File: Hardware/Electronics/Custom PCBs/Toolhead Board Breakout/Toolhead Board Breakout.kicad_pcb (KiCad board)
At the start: 2 copper layers, 75 x 75 mm, 31 parts, among them J1 Conn_02x08_Odd_Even, J10 Conn_01x03, J11 Conn_01x03, J12 Conn_01x03, J13 Conn_01x02, J14 Conn_01x04, J15 Conn_01x02, J16 Conn_01x04, J17 Conn_01x02, J18 Conn_01x02, J19 Conn_01x04, J2 Conn_02x08_Odd_Even, J20 Conn_01x04, J21 Conn_01x02, J22 Conn_01x04, J3 Conn_02x08_Odd_Even, J4 Conn_02x04_Odd_Even, J5 Conn_02x04_Odd_Even, J6 Conn_01x04, J7 Conn_01x03, J8 Conn_01x03, J9 Conn_01x03

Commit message: Updated Breakout Board Layout
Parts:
- moved J6 7.46 mm to (104.5, 60.3), turned to -70 degrees
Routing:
- net +24V: track 0.00 -> 45.3 mm
- net +5V: track 0.00 -> 37.8 mm
- net THERM0: track 0.00 -> 34.5 mm, vias 0 -> 1
- net OB2: track 0.00 -> 31.9 mm
- net SERVO3: track 0.00 -> 31.5 mm
- net OA1: track 0.00 -> 30.2 mm
- net SDA: track 0.00 -> 29.9 mm
- net OB1: track 0.00 -> 29.2 mm
- net SCL: track 0.00 -> 29.1 mm
- net SERVO5: track 0.00 -> 28.8 mm
- net D1: track 0.00 -> 27.9 mm
- net SERVO1: track 0.00 -> 27.5 mm
- net SERVO4: track 0.00 -> 27.3 mm
- net OA2: track 0.00 -> 26.0 mm
- net SERVO6: track 0.00 -> 25.0 mm
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
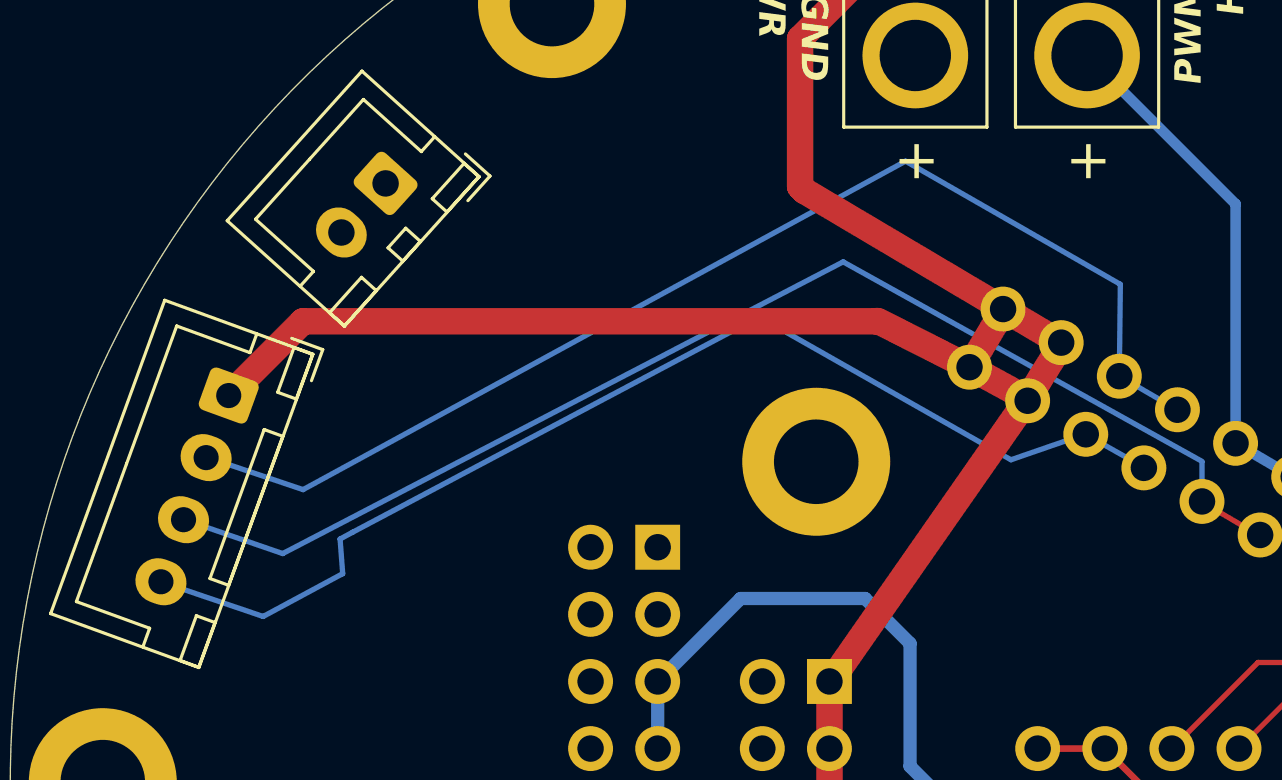
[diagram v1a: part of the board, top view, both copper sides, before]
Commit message: updated breakout board design
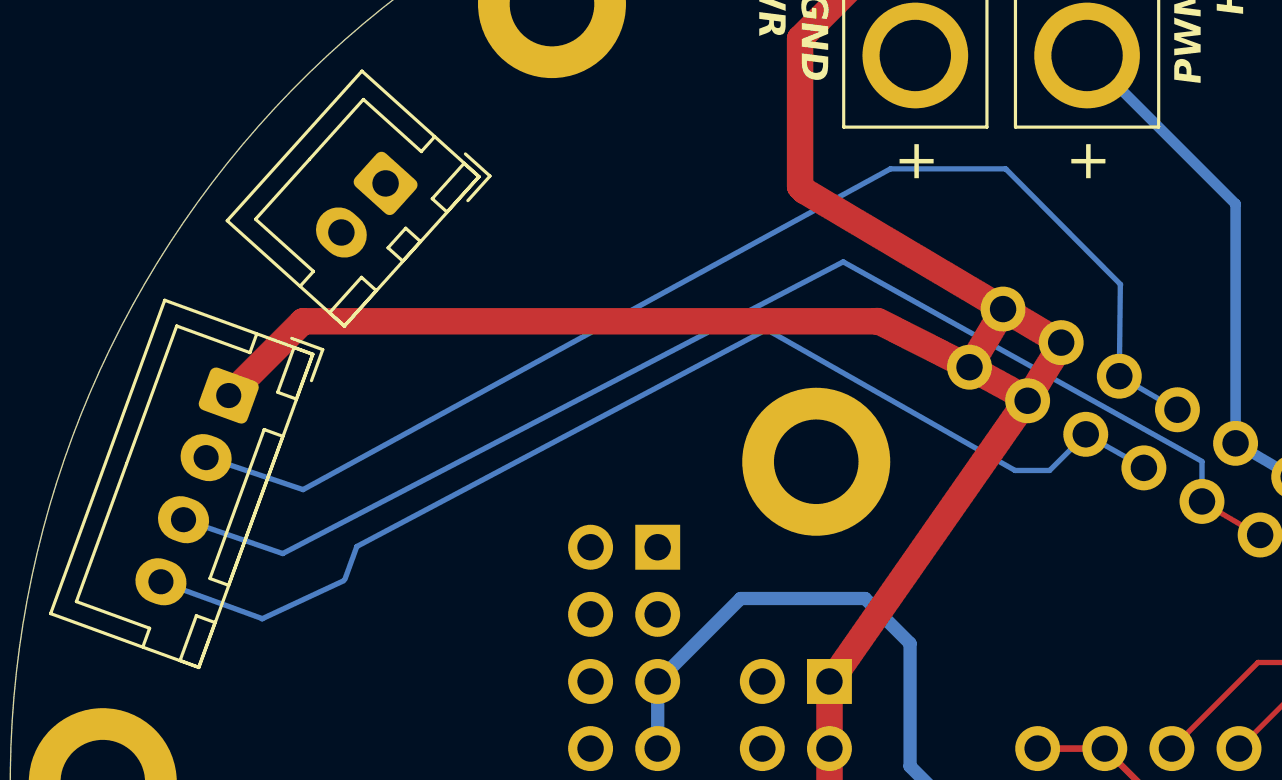
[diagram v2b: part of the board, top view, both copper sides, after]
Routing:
- net 24V_PWM1: track 0.00 -> 4.39 mm
- net 24V_PWM3: track 0.00 -> 3.24 mm
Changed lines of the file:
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@@
-	)
-	(gr_line
-		(start 50.46 65.54)
-		(end 49.98 65.8)
-		(stroke
-			(width 0.2)
-			(type default)
-		)
-		(layer "B.Cu")
-		(net 14)
 	)
 	(gr_line
@@
 	)
 	(gr_line
-		(start 75.37 62.8)
-		(end 65.94 57.45)
+		(start 75.525 63.205)
+		(end 66.095 57.855)
 		(stroke
 			(width 0.2)
@@
 	)
 	(gr_line
-		(start 78.18 61.83)
-		(end 75.37 62.8)
-		(stroke
-			(width 0.2)
-			(type default)
-		)
-		(layer "B.Cu")
-		(net 14)
-	)
-	(gr_line
 		(start 81.48 104.3)
 		(end 81.88 106.7)
@@
 	(gr_line
 		(start 48.58 63.93)
-		(end 71.38 51.5)
+		(end 70.81 51.79)
 		(stroke
 			(width 0.2)
@@
 	(gr_line
 		(start 43.21 67.42)
-		(end 47.07 68.73)
+		(end 47.040409 68.814155)
 		(stroke
 			(width 0.2)
@@
 	)
 	(gr_line
-		(start 71.38 51.5)
-		(end 79.51 56.16)
+		(start 75.19 51.81)
+		(end 79.523089 56.173089)
 		(stroke
 			(width 0.2)
@@
 	)
 	(gr_line
-		(start 50.08 67.11)
-		(end 49.98 65.8)
+		(start 50.165325 67.317289)
+		(end 50.614675 66.08271)
 		(stroke
 			(width 0.2)
@@
 	)
 	(gr_line
-		(start 65.94 57.34)
-		(end 50.46 65.54)
+		(start 66.094675 57.88271)
+		(end 50.614675 66.08271)
 		(stroke
 			(width 0.2)
@@
 	)
 	(gr_line
-		(start 47.07 68.73)
-		(end 50.08 67.11)
+		(start 47.021002 68.822309)
+		(end 50.118998 67.37769)
 		(stroke
 			(width 0.2)
@@
 	)
 	(segment
+		(start 75.17 51.79)
+		(end 75.19 51.81)
+		(width 0.2)
+		(layer "B.Cu")
+		(net 12)
+	)
+	(segment
+		(start 70.81 51.79)
+		(end 75.17 51.79)
+		(width 0.2)
+		(layer "B.Cu")
+		(net 12)
+	)
+	(segment
 		(start 82.599852 64.37667)
 		(end 82.599852 62.890148)
@@
 	)
 	(segment
+		(start 76.832113 63.205)
+		(end 78.200443 61.83667)
+		(width 0.2)
+		(layer "B.Cu")
+		(net 14)
+	)
+	(segment
+		(start 75.525 63.205)
+		(end 76.832113 63.205)
+		(width 0.2)
+		(layer "B.Cu")
+		(net 14)
+	)
+	(segment

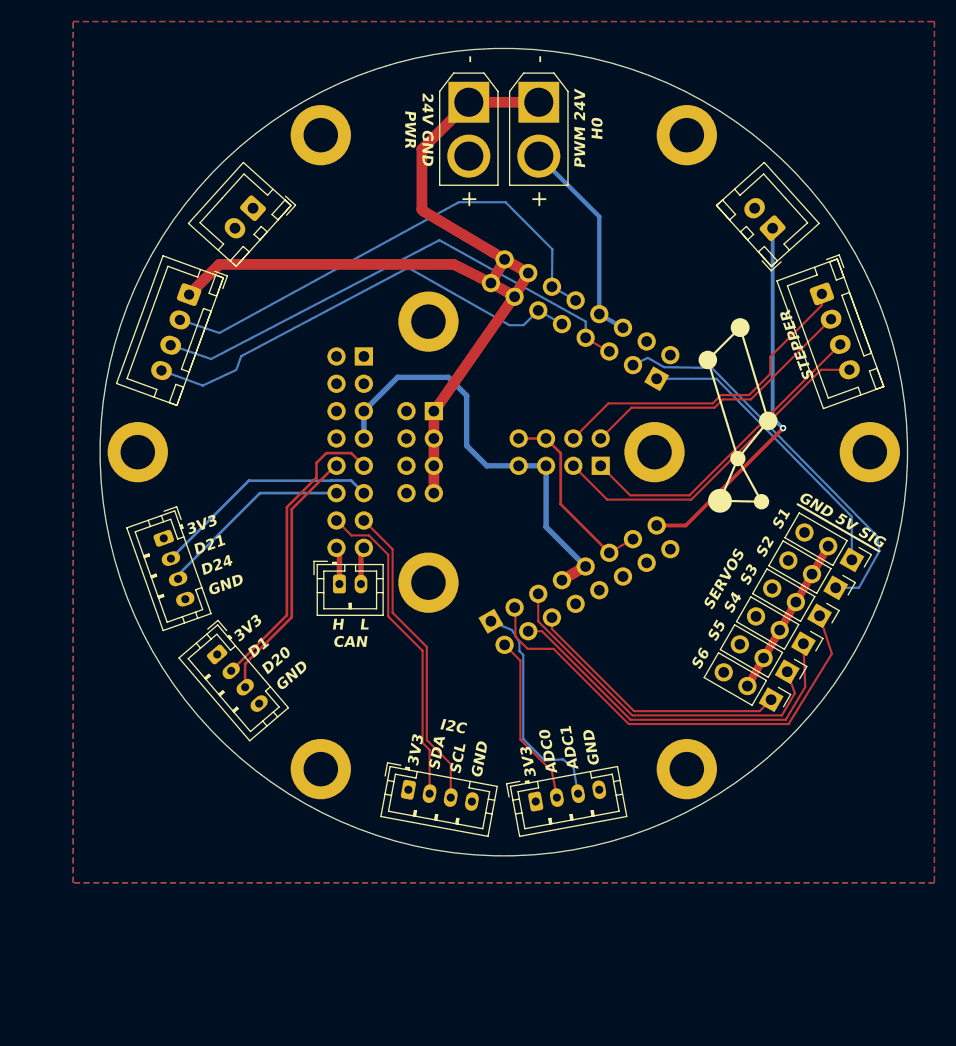
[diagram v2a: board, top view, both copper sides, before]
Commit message: Updated Breakout Board Layout
Finished all the traces. Prior to adding LDO's from 24V to 5V.
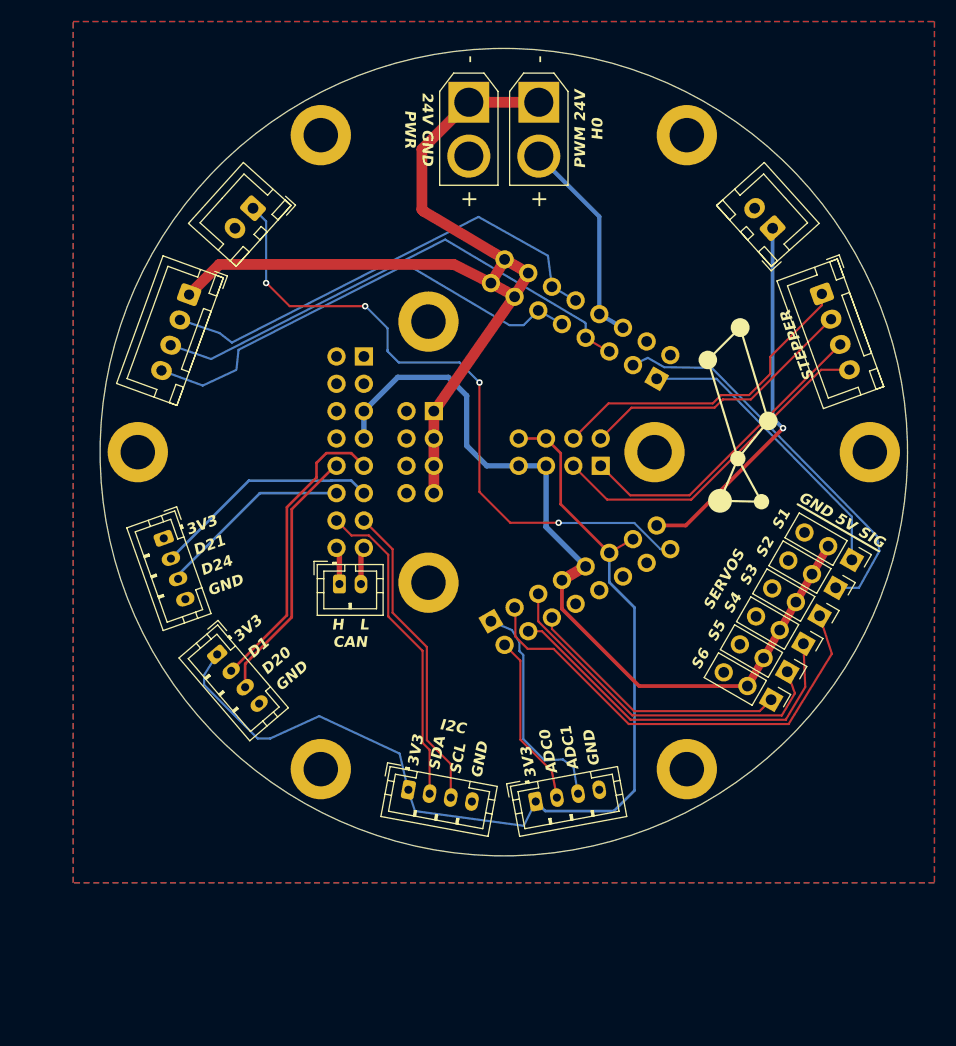
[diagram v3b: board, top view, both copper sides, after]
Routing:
- net THERM1: track 0.00 -> 62.9 mm, vias 0 -> 4
- net +3.3V: track 15.6 -> 58.1 mm
- net +5V: track 37.8 -> 60.6 mm
- net 24V_PWM1: track 4.39 -> 0.00 mm

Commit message: Finished Breakout Board
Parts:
- added C1: 10uF, Capacitor_SMD:C_0805_2012Metric_Pad1.18x1.45mm_HandSolder, F.Cu at (60.0, 54.9)
- added C2: 10uF, Capacitor_SMD:C_0805_2012Metric_Pad1.18x1.45mm_HandSolder, B.Cu at (56.2, 60.1)
- added R1: 5k, Potentiometer_SMD:Potentiometer_Bourns_TC33X_Vertical, F.Cu at (52.3, 60.7)
- added R2: 121, Resistor_SMD:R_0805_2012Metric_Pad1.20x1.40mm_HandSolder, F.Cu at (62.1, 54.9)
- added U1: LM1084-5.0, Package_TO_SOT_SMD:TO-263-3_TabPin2, B.Cu at (51.1, 74.7)
- renumbered H4 to H1, H3 to H1, H8 to H2, H9 to H2, H6 to H2, H7 to H2, H5 to H2
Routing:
- net +5V: track 60.6 -> 92.2 mm, vias 0 -> 3
- net +24V: track 45.3 -> 62.7 mm, vias 0 -> 1
- net Net-(U1-GND): track 0.00 -> 15.5 mm, vias 0 -> 3
- net 24V_PWM1: track 0.00 -> 10.4 mm
- net 24V_PWM2: track 1.49 -> 9.01 mm
- net 24V_PWM3: track 3.24 -> 9.32 mm
- net THERM1: track 62.9 -> 59.7 mm
- net D21: track 21.4 -> 22.3 mm

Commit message: Breakout Board fix
About 60% finished but need some help
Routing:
- net +5V: track 92.2 -> 109.9 mm
- net Net-(U1-GND): track 15.5 -> 14.2 mm

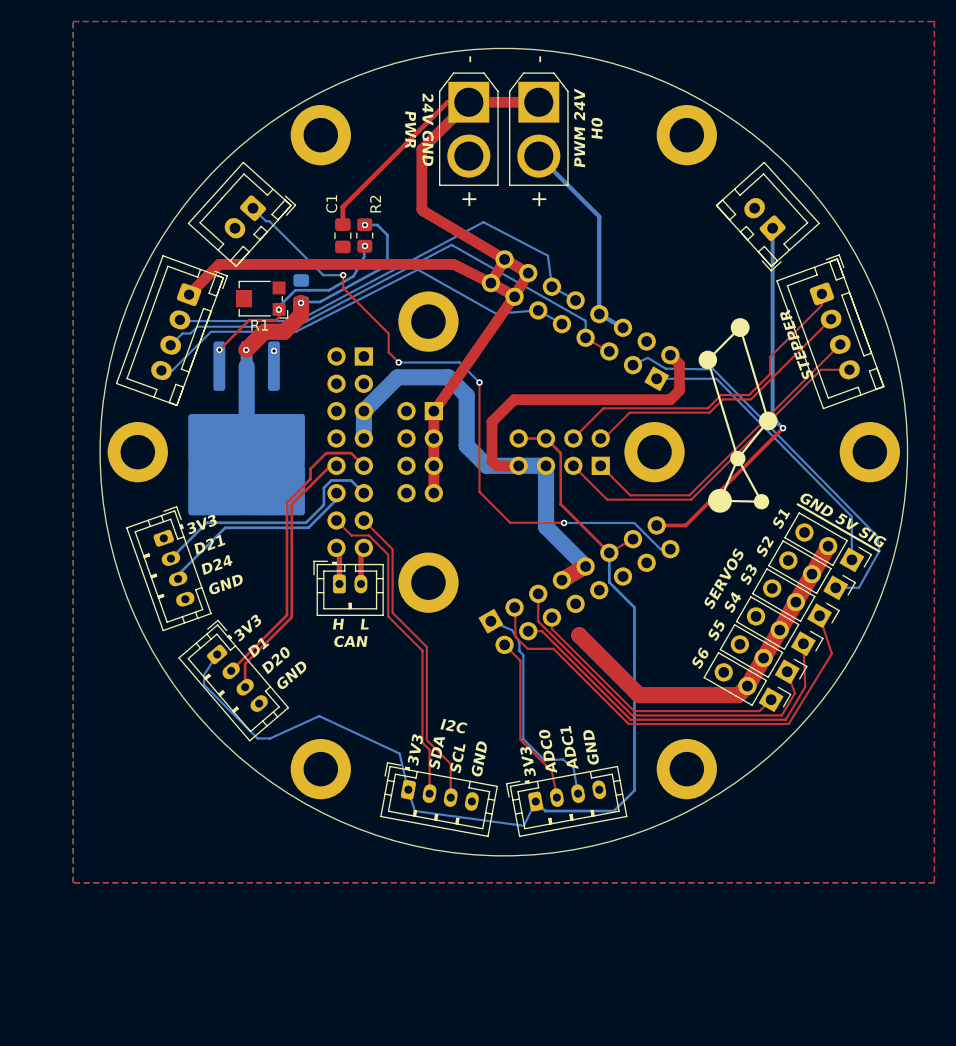
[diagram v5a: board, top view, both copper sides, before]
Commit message: Finish wrist motor mount and update breakout layout
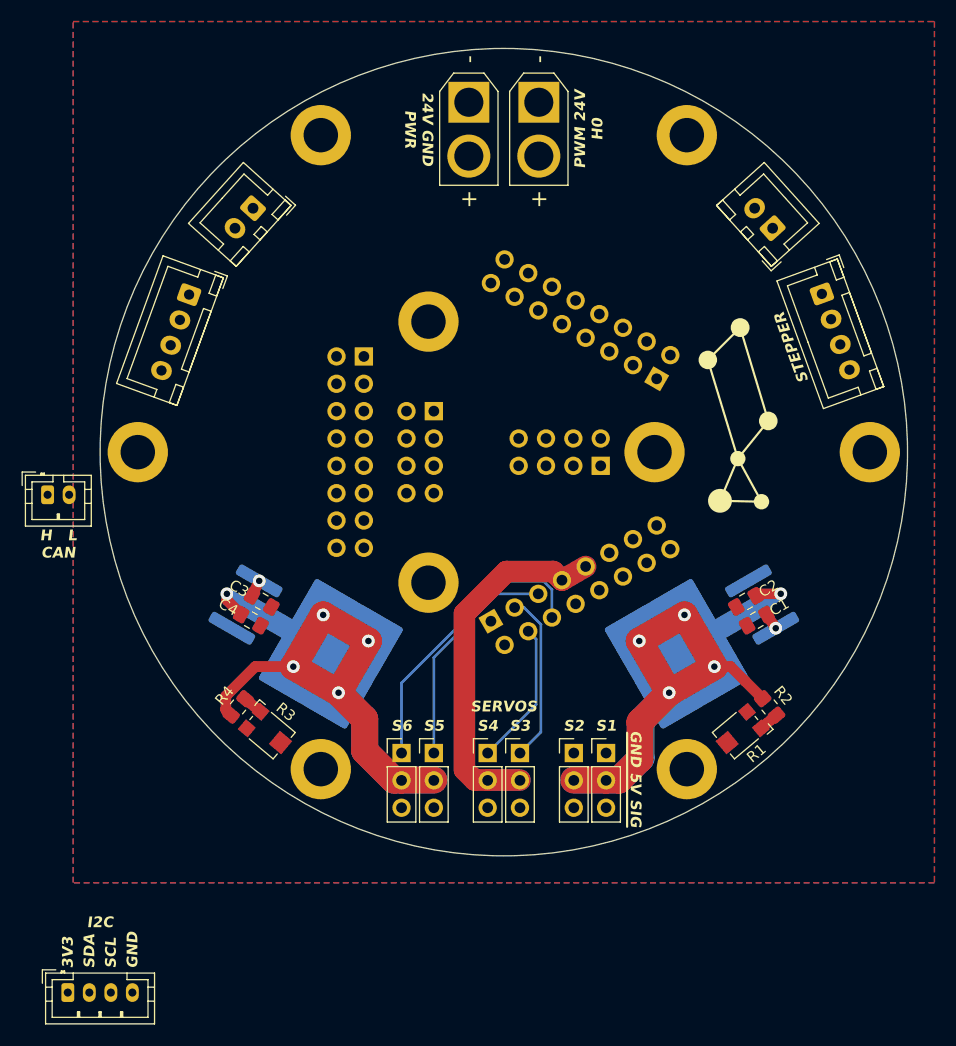
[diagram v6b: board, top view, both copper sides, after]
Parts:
- removed J16, J19, J20: Conn_01x04, Connector_JST:JST_PH_B4B-PH-K_1x04_P2.00mm_Vertical
- added C3: 10uF, Capacitor_SMD:C_0805_2012Metric_Pad1.18x1.45mm_HandSolder, F.Cu at (52.5, 88.9)
- added C4: 10uF, Capacitor_SMD:C_0805_2012Metric_Pad1.18x1.45mm_HandSolder, F.Cu at (51.5, 90.6)
- added R3: 5k, Potentiometer_SMD:Potentiometer_Bourns_TC33X_Vertical, F.Cu at (53.1, 101.0)
- added R4: 121, Resistor_SMD:R_0805_2012Metric_Pad1.20x1.40mm_HandSolder, F.Cu at (50.3, 98.7)
- added U2: LM1084-5.0, Package_TO_SOT_SMD:TO-263-3_TabPin2, B.Cu at (57.6, 93.0)
- C2: moved to F.Cu
- moved R1 60.1 mm to (96.9, 101.0), turned to -140 degrees
- moved R2 57.7 mm to (99.7, 98.7), turned to -50 degrees
- moved C1 52.5 mm to (98.5, 90.6), turned to -150 degrees
- moved C2 50.4 mm to (97.5, 88.9), turned to -150 degrees
- moved U1 45.1 mm to (92.4, 93.0), turned to -150 degrees
- moved J14 36.8 mm to (34.5, 125.2), turned to 0 degrees
- moved J12 34.7 mm to (65.5, 102.9), turned to 0 degrees
- moved J11 33.7 mm to (68.5, 103.0), turned to 0 degrees
- moved J10 31.0 mm to (73.5, 102.9), turned to 0 degrees
- moved J9 30.6 mm to (76.5, 102.9), turned to 0 degrees
- moved J7 29.0 mm to (84.5, 102.9), turned to 0 degrees
- moved J8 28.8 mm to (81.5, 102.9), turned to 0 degrees
- moved J13 28.3 mm to (32.6, 79.0)
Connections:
- C2 pad 1: +5V -> 5VA
- J11 pad 2: +5V -> 5VB
- J12 pad 2: +5V -> 5VB
- J7 pad 2: +5V -> 5VA
- J8 pad 2: +5V -> 5VA
- R2 pad 1: +5V -> 5VA
- U1 pad 2: +5V -> 5VA
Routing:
- net 5VB: track 0.00 -> 90.5 mm, vias 0 -> 5
- net 5VA: track 0.00 -> 87.4 mm, vias 0 -> 5
- net +5V: track 109.9 -> 36.6 mm, vias 3 -> 0
- net THERM1: track 60.0 -> 0.00 mm, vias 4 -> 0
- net +24V: track 62.7 -> 3.09 mm, vias 1 -> 2
- net +3.3V: track 58.1 -> 0.00 mm
- net THERM0: track 34.5 -> 0.00 mm, vias 1 -> 0
- net OB2: track 31.9 -> 0.00 mm
- net OA1: track 30.2 -> 0.00 mm
- net SDA: track 29.9 -> 0.00 mm
- net OB1: track 29.2 -> 0.00 mm
- net SCL: track 29.1 -> 0.00 mm
- net D1: track 27.9 -> 0.00 mm
- net SERVO1: track 27.5 -> 0.00 mm
- net OA2: track 26.0 -> 0.00 mm
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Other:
- board text removed: "ADC0"
- board text removed: "ADC1"
- board text removed: "D1"
- board text removed: "D20"
- board text removed: "D21"
- board text removed: "D24"

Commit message: Finish breakout layout
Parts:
- moved J14 52.8 mm to (54.5, 76.3), turned to 90 degrees
- moved J13 22.3 mm to (54.5, 83.2), turned to 90 degrees
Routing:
- net +24V: track 3.09 -> 157.6 mm
- net THERM1: track 0.00 -> 84.1 mm, vias 0 -> 2
- net +3.3V: track 0.00 -> 67.9 mm, vias 0 -> 2
- net +5V: track 36.6 -> 90.3 mm
- net SERVO2: track 0.00 -> 47.4 mm, vias 0 -> 2
- net SERVO1: track 0.00 -> 44.0 mm, vias 0 -> 2
- net 24V_PWM2: track 0.00 -> 43.5 mm
- net 24V_PWM1: track 0.00 -> 42.8 mm
- net 24V_PWM3: track 0.00 -> 41.7 mm, vias 0 -> 1
- net 24V_PWM0: track 0.00 -> 36.5 mm
- net THERM0: track 0.00 -> 36.2 mm, vias 0 -> 2
- net OB2: track 0.00 -> 31.9 mm
- net OB1: track 0.00 -> 28.7 mm
- net OA1: track 0.00 -> 28.6 mm
- net OA2: track 0.00 -> 26.0 mm
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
